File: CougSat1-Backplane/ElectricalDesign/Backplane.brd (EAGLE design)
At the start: 82.8 x 86 mm, 17 parts, among them J1 CougSat Socket, J10 CougSat Socket, J2 CougSat Socket, J3 CougSat Socket, J4 CougSat Socket, J5 Separation Switch, J6 Separation Switch, J7 CougSat Socket, J8 CougSat Socket, J9 CougSat Socket

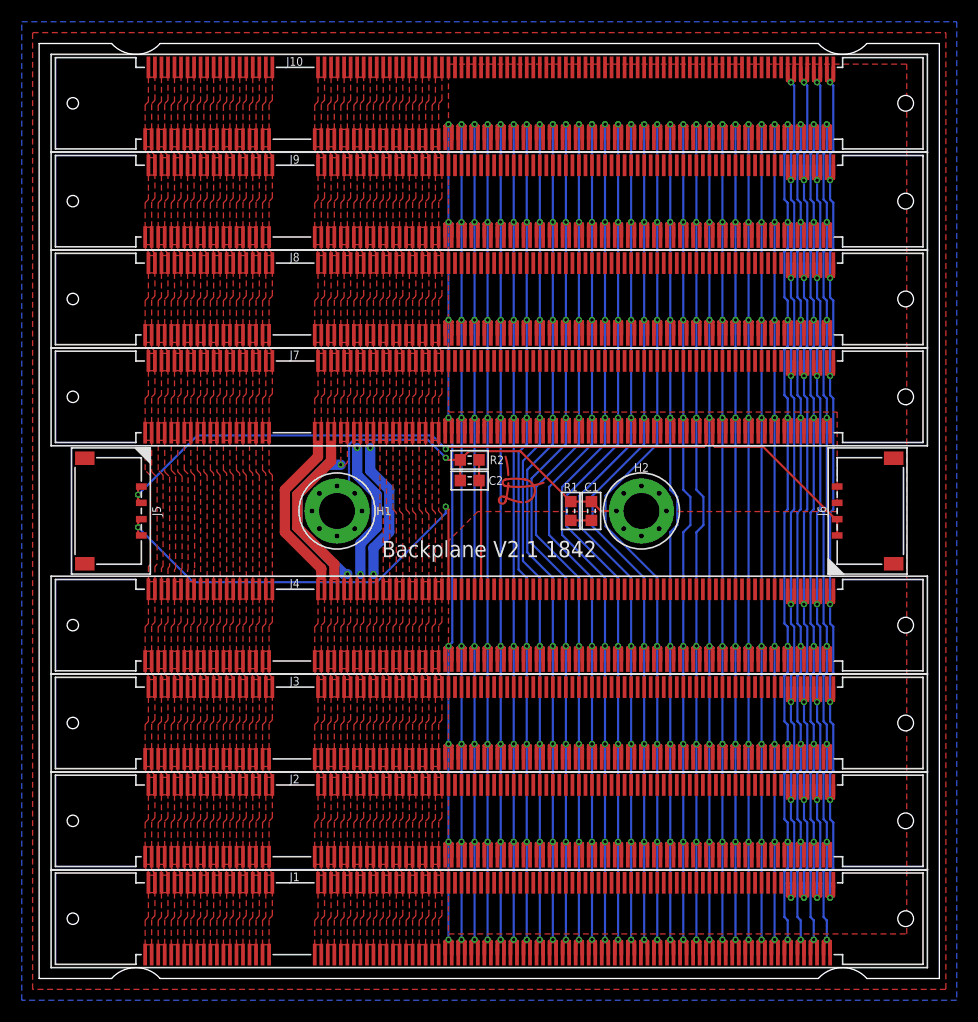
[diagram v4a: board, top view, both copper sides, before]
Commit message: Changed Cutout for Solar Panel Mount
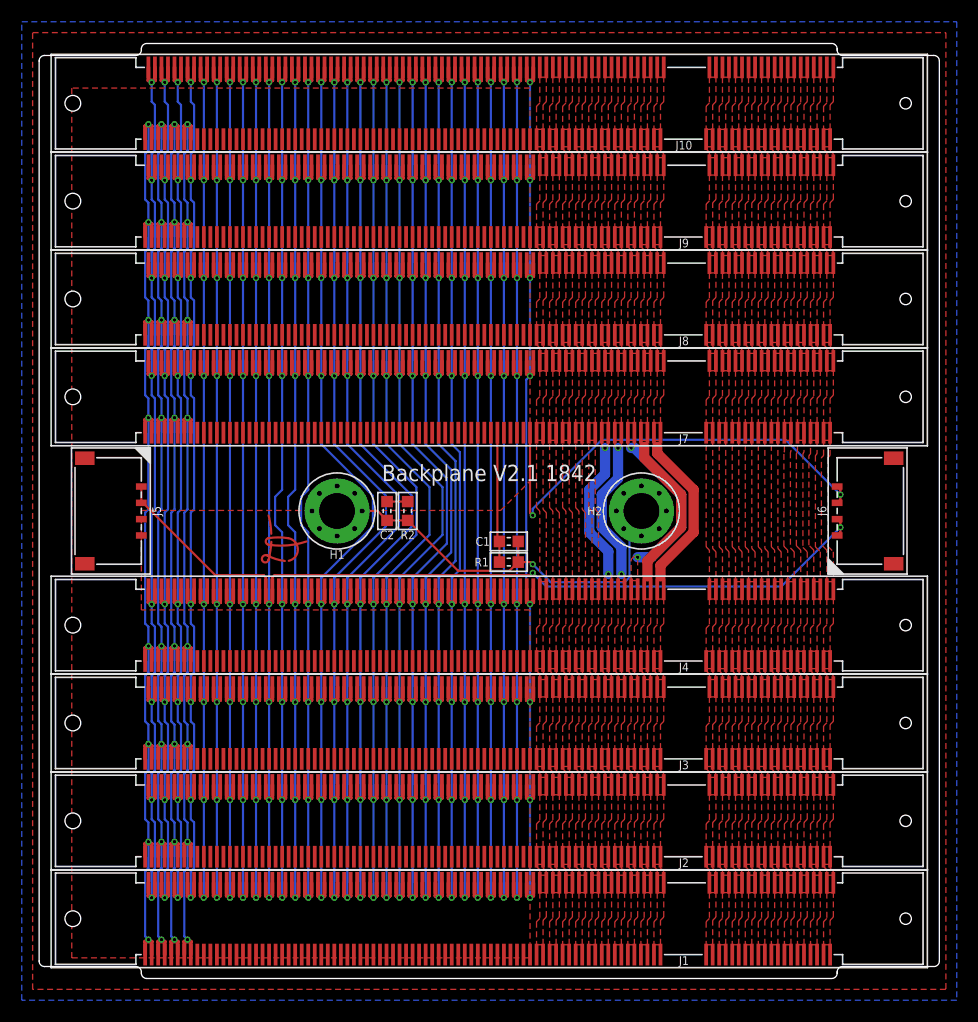
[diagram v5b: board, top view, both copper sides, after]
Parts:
- moved LOGO1 22.5 mm to (-18.8, -2.60)
- moved C1 8.10 mm to (1.80, -2.80), turned to 180 degrees
- moved C2 8.10 mm to (-9.40, 0.00), turned to 90 degrees
- moved R1 7.39 mm to (1.80, -4.70), turned to 0 degrees
- moved R2 7.39 mm to (-7.50, 0.00), turned to 270 degrees
- turned H1 to 180 degrees
- turned H2 to 180 degrees
- turned J1 to 180 degrees
- turned J10 to 180 degrees
- turned J2 to 180 degrees
- turned J3 to 180 degrees
- turned J4 to 180 degrees
- turned J7 to 180 degrees
- turned J8 to 180 degrees
- turned J9 to 180 degrees
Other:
- outline, holes or cut-outs redrawn

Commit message: Merge branch 'master' into panel+X
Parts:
- added LOGO100, LOGO3: Satellite 16mm, CougsInSpace-Aesthetics:CIS-SATELLITE-16
- added LOGO2: SIGNATUREHENDRIK, CougsInSpace-Aesthetics:SIGN-HENDRIK
- J1, J10, J2, J3, J4, J7, J8, J9: device CougsInSpace-Connectors:SODIMM-DDR1 -> CougsInSpace-Connectors:PCIE-8
- LOGO1: value SIGNATUREBRADLEY -> Text; device CougsInSpace-Aesthetics:SIGN-BRADLEY -> CougsInSpace-Aesthetics:CIS-TEXT
- moved J1 78.7 mm to (24.0, 37.5)
- moved J10 78.7 mm to (24.0, -37.5)
- moved J2 61.8 mm to (24.0, 28.5)
- moved J9 61.8 mm to (24.0, -28.5)
- moved J3 45.8 mm to (24.0, 19.5)
- moved J8 45.8 mm to (24.0, -19.5)
- moved J4 31.9 mm to (24.0, 10.5)
- moved J7 31.9 mm to (24.0, -10.5)
- moved C2 19.0 mm to (9.50, -1.80), turned to 270 degrees
- moved R2 17.1 mm to (9.50, 1.80)
- moved R1 13.0 mm to (-9.50, 1.80), turned to 270 degrees
- moved C1 11.3 mm to (-9.50, -1.80), turned to 270 degrees
- moved LOGO1 9.97 mm to (-28.4, 0.10), flipped to the bottom, turned to 90 degrees
- moved J5 3.00 mm to (-29.0, 0.00)
- moved J6 3.00 mm to (29.0, 0.00)
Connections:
- removed net CHASSIS: C1.1, C2.1, H1.1, H1.V1, H1.V2, H1.V3, H1.V4, H1.V5, H1.V6, H1.V7, H1.V8, H2.1, H2.V1, H2.V2, H2.V3, H2.V4, H2.V5, H2.V6, H2.V7, H2.V8, R1.2, R2.2
- removed net GPIO-6: J1.105, J1.107, J10.105, J10.107, J2.105, J2.107, J3.105, J3.107, J4.105, J4.107, J7.105, J7.107, J8.105, J8.107, J9.105, J9.107
- removed net GPIO-7: J1.109, J1.111, J10.109, J10.111, J2.109, J2.111, J3.109, J3.111, J4.109, J4.111, J7.109, J7.111, J8.109, J8.111, J9.109, J9.111
- removed net GPIO-8: J1.113, J1.115, J10.113, J10.115, J2.113, J2.115, J3.113, J3.115, J4.113, J4.115, J7.113, J7.115, J8.113, J8.115, J9.113, J9.115
- removed net GPIO-9: J1.117, J1.119, J10.117, J10.119, J2.117, J2.119, J3.117, J3.119, J4.117, J4.119, J7.117, J7.119, J8.117, J8.119, J9.117, J9.119
- new net CHASSIS1: C1.1, H1.1, H1.V1, H1.V2, H1.V3, H1.V4, H1.V5, H1.V6, H1.V7, H1.V8, R1.2
- new net CHASSIS2: C2.1, H2.1, H2.V1, H2.V2, H2.V3, H2.V4, H2.V5, H2.V6, H2.V7, H2.V8, R2.2
- net BUS_I2C0_IRQ: now also J1.A45, J1.B45, J10.A45, J10.B45, J2.A45, J2.B45, J3.A45, J3.B45, J4.A45, J4.B45, J7.A45, J7.B45, J8.A45, J8.B45, J9.A45, J9.B45; no longer J1.181, J1.183, J10.181, J10.183, J2.181, J2.183, J3.181, J3.183, J4.181, J4.183, J7.181, J7.183, J8.181, J8.183, J9.181, J9.183
- net BUS_I2C0_SCL: now also J1.A44, J1.B44, J10.A44, J10.B44, J2.A44, J2.B44, J3.A44, J3.B44, J4.A44, J4.B44, J7.A44, J7.B44, J8.A44, J8.B44, J9.A44, J9.B44; no longer J1.177, J1.179, J10.177, J10.179, J2.177, J2.179, J3.177, J3.179, J4.177, J4.179, J7.177, J7.179, J8.177, J8.179, J9.177, J9.179
- net BUS_I2C0_SDA: now also J1.A43, J1.B43, J10.A43, J10.B43, J2.A43, J2.B43, J3.A43, J3.B43, J4.A43, J4.B43, J7.A43, J7.B43, J8.A43, J8.B43, J9.A43, J9.B43; no longer J1.173, J1.175, J10.173, J10.175, J2.173, J2.175, J3.173, J3.175, J4.173, J4.175, J7.173, J7.175, J8.173, J8.175, J9.173, J9.175
- net BUS_I2C1_IRQ: now also J1.A32, J1.B32, J10.A32, J10.B32, J2.A32, J2.B32, J3.A32, J3.B32, J4.A32, J4.B32, J7.A32, J7.B32, J8.A32, J8.B32, J9.A32, J9.B32; no longer J1.129, J1.131, J10.129, J10.131, J2.129, J2.131, J3.129, J3.131, J4.129, J4.131, J7.129, J7.131, J8.129, J8.131, J9.129, J9.131
- net BUS_I2C1_SCL: now also J1.A31, J1.B31, J10.A31, J10.B31, J2.A31, J2.B31, J3.A31, J3.B31, J4.A31, J4.B31, J7.A31, J7.B31, J8.A31, J8.B31, J9.A31, J9.B31; no longer J1.125, J1.127, J10.125, J10.127, J2.125, J2.127, J3.125, J3.127, J4.125, J4.127, J7.125, J7.127, J8.125, J8.127, J9.125, J9.127
- net BUS_I2C1_SDA: now also J1.A30, J1.B30, J10.A30, J10.B30, J2.A30, J2.B30, J3.A30, J3.B30, J4.A30, J4.B30, J7.A30, J7.B30, J8.A30, J8.B30, J9.A30, J9.B30; no longer J1.121, J1.123, J10.121, J10.123, J2.121, J2.123, J3.121, J3.123, J4.121, J4.123, J7.121, J7.123, J8.121, J8.123, J9.121, J9.123
- net BUS_JTAG_EN-0: now also J1.B46, J10.B46, J2.B46, J3.B46, J4.B46, J7.B46, J8.B46, J9.B46; no longer J1.186, J1.188, J10.186, J10.188, J2.186, J2.188, J3.186, J3.188, J4.186, J4.188, J7.186, J7.188, J8.186, J8.188, J9.186, J9.188
- net BUS_JTAG_EN-1: now also J1.B47, J10.B47, J2.B47, J3.B47, J4.B47, J7.B47, J8.B47, J9.B47; no longer J1.190, J1.192, J10.190, J10.192, J2.190, J2.192, J3.190, J3.192, J4.190, J4.192, J7.190, J7.192, J8.190, J8.192, J9.190, J9.192
- net BUS_JTAG_EN-2: now also J1.B48, J10.B48, J2.B48, J3.B48, J4.B48, J7.B48, J8.B48, J9.B48; no longer J1.194, J1.196, J10.194, J10.196, J2.194, J2.196, J3.194, J3.196, J4.194, J4.196, J7.194, J7.196, J8.194, J8.196, J9.194, J9.196
- net BUS_JTAG_EN-3: now also J1.B49, J10.B49, J2.B49, J3.B49, J4.B49, J7.B49, J8.B49, J9.B49; no longer J1.198, J1.200, J10.198, J10.200, J2.198, J2.200, J3.198, J3.200, J4.198, J4.200, J7.198, J7.200, J8.198, J8.200, J9.198, J9.200
- net BUS_JTAG_TCK: now also J1.A46, J10.A46, J2.A46, J3.A46, J4.A46, J7.A46, J8.A46, J9.A46; no longer J1.185, J1.187, J10.185, J10.187, J2.185, J2.187, J3.185, J3.187, J4.185, J4.187, J7.185, J7.187, J8.185, J8.187, J9.185, J9.187
- net BUS_JTAG_TDI: now also J1.A47, J10.A47, J2.A47, J3.A47, J4.A47, J7.A47, J8.A47, J9.A47; no longer J1.189, J1.191, J10.189, J10.191, J2.189, J2.191, J3.189, J3.191, J4.189, J4.191, J7.189, J7.191, J8.189, J8.191, J9.189, J9.191
- net BUS_JTAG_TDO: now also J1.A48, J10.A48, J2.A48, J3.A48, J4.A48, J7.A48, J8.A48, J9.A48; no longer J1.193, J1.195, J10.193, J10.195, J2.193, J2.195, J3.193, J3.195, J4.193, J4.195, J7.193, J7.195, J8.193, J8.195, J9.193, J9.195
- net BUS_JTAG_TMS: now also J1.A49, J10.A49, J2.A49, J3.A49, J4.A49, J7.A49, J8.A49, J9.A49; no longer J1.197, J1.199, J10.197, J10.199, J2.197, J2.199, J3.197, J3.199, J4.197, J4.199, J7.197, J7.199, J8.197, J8.199, J9.197, J9.199
- net BUS_SPI_MISO: now also J1.A38, J1.B38, J10.A38, J10.B38, J2.A38, J2.B38, J3.A38, J3.B38, J4.A38, J4.B38, J7.A38, J7.B38, J8.A38, J8.B38, J9.A38, J9.B38; no longer J1.153, J1.155, J10.153, J10.155, J2.153, J2.155, J3.153, J3.155, J4.153, J4.155, J7.153, J7.155, J8.153, J8.155, J9.153, J9.155
- net BUS_SPI_MOSI: now also J1.A39, J1.B39, J10.A39, J10.B39, J2.A39, J2.B39, J3.A39, J3.B39, J4.A39, J4.B39, J7.A39, J7.B39, J8.A39, J8.B39, J9.A39, J9.B39; no longer J1.157, J1.159, J10.157, J10.159, J2.157, J2.159, J3.157, J3.159, J4.157, J4.159, J7.157, J7.159, J8.157, J8.159, J9.157, J9.159
- net BUS_SPI_SCK: now also J1.A37, J1.B37, J10.A37, J10.B37, J2.A37, J2.B37, J3.A37, J3.B37, J4.A37, J4.B37, J7.A37, J7.B37, J8.A37, J8.B37, J9.A37, J9.B37; no longer J1.149, J1.151, J10.149, J10.151, J2.149, J2.151, J3.149, J3.151, J4.149, J4.151, J7.149, J7.151, J8.149, J8.151, J9.149, J9.151
- net COM_SPI_CS: now also J1.A36, J1.B36, J10.A36, J10.B36, J2.A36, J2.B36, J3.A36, J3.B36, J4.A36, J4.B36, J7.A36, J7.B36, J8.A36, J8.B36, J9.A36, J9.B36; no longer J1.145, J1.147, J10.145, J10.147, J2.145, J2.147, J3.145, J3.147, J4.145, J4.147, J7.145, J7.147, J8.145, J8.147, J9.145, J9.147
- net COM_SPI_MISO: now also J1.A34, J1.B34, J10.A34, J10.B34, J2.A34, J2.B34, J3.A34, J3.B34, J4.A34, J4.B34, J7.A34, J7.B34, J8.A34, J8.B34, J9.A34, J9.B34; no longer J1.137, J1.139, J10.137, J10.139, J2.137, J2.139, J3.137, J3.139, J4.137, J4.139, J7.137, J7.139, J8.137, J8.139, J9.137, J9.139
- net COM_SPI_MOSI: now also J1.A35, J1.B35, J10.A35, J10.B35, J2.A35, J2.B35, J3.A35, J3.B35, J4.A35, J4.B35, J7.A35, J7.B35, J8.A35, J8.B35, J9.A35, J9.B35; no longer J1.141, J1.143, J10.141, J10.143, J2.141, J2.143, J3.141, J3.143, J4.141, J4.143, J7.141, J7.143, J8.141, J8.143, J9.141, J9.143
- net COM_SPI_SCK: now also J1.A33, J1.B33, J10.A33, J10.B33, J2.A33, J2.B33, J3.A33, J3.B33, J4.A33, J4.B33, J7.A33, J7.B33, J8.A33, J8.B33, J9.A33, J9.B33; no longer J1.133, J1.135, J10.133, J10.135, J2.133, J2.135, J3.133, J3.135, J4.133, J4.135, J7.133, J7.135, J8.133, J8.135, J9.133, J9.135
- net CTRL_!RESET: now also J1.A41, J1.B41, J10.A41, J10.B41, J2.A41, J2.B41, J3.A41, J3.B41, J4.A41, J4.B41, J7.A41, J7.B41, J8.A41, J8.B41, J9.A41, J9.B41; no longer J1.165, J1.167, J10.165, J10.167, J2.165, J2.167, J3.165, J3.167, J4.165, J4.167, J7.165, J7.167, J8.165, J8.167, J9.165, J9.167
- net CTRL_SYNC: now also J1.A42, J1.B42, J10.A42, J10.B42, J2.A42, J2.B42, J3.A42, J3.B42, J4.A42, J4.B42, J7.A42, J7.B42, J8.A42, J8.B42, J9.A42, J9.B42; no longer J1.169, J1.171, J10.169, J10.171, J2.169, J2.171, J3.169, J3.171, J4.169, J4.171, J7.169, J7.171, J8.169, J8.171, J9.169, J9.171
- net GPIO-0: now also J1.A24, J10.A24, J2.A24, J3.A24, J4.A24, J7.A24, J8.A24, J9.A24; no longer J1.81, J1.83, J10.81, J10.83, J2.81, J2.83, J3.81, J3.83, J4.81, J4.83, J7.81, J7.83, J8.81, J8.83, J9.81, J9.83
- net GPIO-1: now also J1.A25, J10.A25, J2.A25, J3.A25, J4.A25, J7.A25, J8.A25, J9.A25; no longer J1.85, J1.87, J10.85, J10.87, J2.85, J2.87, J3.85, J3.87, J4.85, J4.87, J7.85, J7.87, J8.85, J8.87, J9.85, J9.87
- net GPIO-2: now also J1.A26, J10.A26, J2.A26, J3.A26, J4.A26, J7.A26, J8.A26, J9.A26; no longer J1.89, J1.91, J10.89, J10.91, J2.89, J2.91, J3.89, J3.91, J4.89, J4.91, J7.89, J7.91, J8.89, J8.91, J9.89, J9.91
- net GPIO-3: now also J1.A27, J10.A27, J2.A27, J3.A27, J4.A27, J7.A27, J8.A27, J9.A27; no longer J1.93, J1.95, J10.93, J10.95, J2.93, J2.95, J3.93, J3.95, J4.93, J4.95, J7.93, J7.95, J8.93, J8.95, J9.93, J9.95
- net GPIO-4: now also J1.A28, J10.A28, J2.A28, J3.A28, J4.A28, J7.A28, J8.A28, J9.A28; no longer J1.97, J1.99, J10.97, J10.99, J2.97, J2.99, J3.97, J3.99, J4.97, J4.99, J7.97, J7.99, J8.97, J8.99, J9.97, J9.99
- net GPIO-5: now also J1.A29, J10.A29, J2.A29, J3.A29, J4.A29, J7.A29, J8.A29, J9.A29; no longer J1.101, J1.103, J10.101, J10.103, J2.101, J2.103, J3.101, J3.103, J4.101, J4.103, J7.101, J7.103, J8.101, J8.103, J9.101, J9.103
- net PGND: now also J1.A21, J1.A22, J1.A23, J1.B21, J1.B22, J1.B23, J1.B24, J1.B25, J1.B26, J1.B27, J1.B28, J1.B29, J10.A21, J10.A22, J10.A23, J10.B21, J10.B22, J10.B23, J10.B24, J10.B25, J10.B26, J10.B27, J10.B28, J10.B29, J2.A21, J2.A22, J2.A23, J2.B21, J2.B22, J2.B23, J2.B24, J2.B25, J2.B26, J2.B27, J2.B28, J2.B29, J3.A21, J3.A22, J3.A23, J3.B21, J3.B22, J3.B23, J3.B24, J3.B25, J3.B26, J3.B27, J3.B28, J3.B29, J4.A21, J4.A22, J4.A23, J4.B21, J4.B22, J4.B23, J4.B24, J4.B25, J4.B26, J4.B27, J4.B28, J4.B29, J7.A21, J7.A22, J7.A23, J7.B21, J7.B22, J7.B23, J7.B24, J7.B25, J7.B26, J7.B27, J7.B28, J7.B29, J8.A21, J8.A22, J8.A23, J8.B21, J8.B22, J8.B23, J8.B24, J8.B25, J8.B26, J8.B27, J8.B28, J8.B29, J9.A21, J9.A22, J9.A23, J9.B21, J9.B22, J9.B23, J9.B24, J9.B25, J9.B26, J9.B27, J9.B28, J9.B29; no longer J1.100, J1.102, J1.104, J1.106, J1.108, J1.110, J1.112, J1.114, J1.116, J1.118, J1.120, J1.122, J1.124, J1.126, J1.128, J1.130, J1.132, J1.134, J1.136, J1.138, J1.140, J1.142, J1.144, J1.146, J1.148, J1.150, J1.152, J1.154, J1.156, J1.158, J1.160, J1.162, J1.164, J1.166, J1.168, J1.170, J1.172, J1.174, J1.176, J1.178, J1.180, J1.182, J1.184, J1.82, J1.84, J1.86, J1.88, J1.90, J1.92, J1.94, J1.96, J1.98, J10.100, J10.102, J10.104, J10.106, J10.108, J10.110, J10.112, J10.114, J10.116, J10.118, J10.120, J10.122, J10.124, J10.126, J10.128, J10.130, J10.132, J10.134, J10.136, J10.138, J10.140, J10.142, J10.144, J10.146, J10.148, J10.150, J10.152, J10.154, J10.156, J10.158, J10.160, J10.162, J10.164, J10.166, J10.168, J10.170, J10.172, J10.174, J10.176, J10.178, J10.180, J10.182, J10.184, J10.82, J10.84, J10.86, J10.88, J10.90, J10.92, J10.94, J10.96, J10.98, J2.100, J2.102, J2.104, J2.106, J2.108, J2.110, J2.112, J2.114, J2.116, J2.118, J2.120, J2.122, J2.124, J2.126, J2.128, J2.130, J2.132, J2.134, J2.136, J2.138, J2.140, J2.142, J2.144, J2.146, J2.148, J2.150, J2.152, J2.154, J2.156, J2.158, J2.160, J2.162, J2.164, J2.166, J2.168, J2.170, J2.172, J2.174, J2.176, J2.178, J2.180, J2.182, J2.184, J2.82, J2.84, J2.86, J2.88, J2.90, J2.92, J2.94, J2.96, J2.98, J3.100, J3.102, J3.104, J3.106, J3.108, J3.110, J3.112, J3.114, J3.116, J3.118, J3.120, J3.122, J3.124, J3.126, J3.128, J3.130, J3.132, J3.134, J3.136, J3.138, J3.140, J3.142, J3.144, J3.146, J3.148, J3.150, J3.152, J3.154, J3.156, J3.158, J3.160, J3.162, J3.164, J3.166, J3.168, J3.170, J3.172, J3.174, J3.176, J3.178, J3.180, J3.182, J3.184, J3.82, J3.84, J3.86, J3.88, J3.90, J3.92, J3.94, J3.96, J3.98, J4.100, J4.102, J4.104, J4.106, J4.108, J4.110, J4.112, J4.114, J4.116, J4.118, J4.120, J4.122, J4.124, J4.126, J4.128, J4.130, J4.132, J4.134, J4.136, J4.138, J4.140, J4.142, J4.144, J4.146, J4.148, J4.150, J4.152, J4.154, J4.156, J4.158, J4.160, J4.162, J4.164, J4.166, J4.168, J4.170, J4.172, J4.174, J4.176, J4.178, J4.180, J4.182, J4.184, J4.82, J4.84, J4.86, J4.88, J4.90, J4.92, J4.94, J4.96, J4.98, J7.100, J7.102, J7.104, J7.106, J7.108, J7.110, J7.112, J7.114, J7.116, J7.118, J7.120, J7.122, J7.124, J7.126, J7.128, J7.130, J7.132, J7.134, J7.136, J7.138, J7.140, J7.142, J7.144, J7.146, J7.148, J7.150, J7.152, J7.154, J7.156, J7.158, J7.160, J7.162, J7.164, J7.166, J7.168, J7.170, J7.172, J7.174, J7.176, J7.178, J7.180, J7.182, J7.184, J7.82, J7.84, J7.86, J7.88, J7.90, J7.92, J7.94, J7.96, J7.98, J8.100, J8.102, J8.104, J8.106, J8.108, J8.110, J8.112, J8.114, J8.116, J8.118, J8.120, J8.122, J8.124, J8.126, J8.128, J8.130, J8.132, J8.134, J8.136, J8.138, J8.140, J8.142, J8.144, J8.146, J8.148, J8.150, J8.152, J8.154, J8.156, J8.158, J8.160, J8.162, J8.164, J8.166, J8.168, J8.170, J8.172, J8.174, J8.176, J8.178, J8.180, J8.182, J8.184, J8.82, J8.84, J8.86, J8.88, J8.90, J8.92, J8.94, J8.96, J8.98, J9.100, J9.102, J9.104, J9.106, J9.108, J9.110, J9.112, J9.114, J9.116, J9.118, J9.120, J9.122, J9.124, J9.126, J9.128, J9.130, J9.132, J9.134, J9.136, J9.138, J9.140, J9.142, J9.144, J9.146, J9.148, J9.150, J9.152, J9.154, J9.156, J9.158, J9.160, J9.162, J9.164, J9.166, J9.168, J9.170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
- net PR_3.3V-0: now also J1.A1, J1.B1, J10.A1, J10.B1, J2.A1, J2.B1, J3.A1, J3.B1, J4.A1, J4.B1, J7.A1, J7.B1, J8.A1, J8.B1, J9.A1, J9.B1; no longer J1.1, J1.2, J1.3, J1.4, J10.1, J10.2, J10.3, J10.4, J2.1, J2.2, J2.3, J2.4, J3.1, J3.2, J3.3, J3.4, J4.1, J4.2, J4.3, J4.4, J7.1, J7.2, J7.3, J7.4, J8.1, J8.2, J8.3, J8.4, J9.1, J9.2, J9.3, J9.4
- net PR_3.3V-1: now also J1.A2, J1.B2, J10.A2, J10.B2, J2.A2, J2.B2, J3.A2, J3.B2, J4.A2, J4.B2, J7.A2, J7.B2, J8.A2, J8.B2, J9.A2, J9.B2; no longer J1.5, J1.6, J1.7, J1.8, J10.5, J10.6, J10.7, J10.8, J2.5, J2.6, J2.7, J2.8, J3.5, J3.6, J3.7, J3.8, J4.5, J4.6, J4.7, J4.8, J7.5, J7.6, J7.7, J7.8, J8.5, J8.6, J8.7, J8.8, J9.5, J9.6, J9.7, J9.8
- net PR_3.3V-10: now also J1.A11, J1.B11, J10.A11, J10.B11, J2.A11, J2.B11, J3.A11, J3.B11, J4.A11, J4.B11, J7.A11, J7.B11, J8.A11, J8.B11, J9.A11, J9.B11; no longer J1.41, J1.42, J1.43, J1.44, J10.41, J10.42, J10.43, J10.44, J2.41, J2.42, J2.43, J2.44, J3.41, J3.42, J3.43, J3.44, J4.41, J4.42, J4.43, J4.44, J7.41, J7.42, J7.43, J7.44, J8.41, J8.42, J8.43, J8.44, J9.41, J9.42, J9.43, J9.44
- net PR_3.3V-11: now also J1.A12, J1.B12, J10.A12, J10.B12, J2.A12, J2.B12, J3.A12, J3.B12, J4.A12, J4.B12, J7.A12, J7.B12, J8.A12, J8.B12, J9.A12, J9.B12; no longer J1.45, J1.46, J1.47, J1.48, J10.45, J10.46, J10.47, J10.48, J2.45, J2.46, J2.47, J2.48, J3.45, J3.46, J3.47, J3.48, J4.45, J4.46, J4.47, J4.48, J7.45, J7.46, J7.47, J7.48, J8.45, J8.46, J8.47, J8.48, J9.45, J9.46, J9.47, J9.48
- net PR_3.3V-12: now also J1.A13, J1.B13, J10.A13, J10.B13, J2.A13, J2.B13, J3.A13, J3.B13, J4.A13, J4.B13, J7.A13, J7.B13, J8.A13, J8.B13, J9.A13, J9.B13; no longer J1.49, J1.50, J1.51, J1.52, J10.49, J10.50, J10.51, J10.52, J2.49, J2.50, J2.51, J2.52, J3.49, J3.50, J3.51, J3.52, J4.49, J4.50, J4.51, J4.52, J7.49, J7.50, J7.51, J7.52, J8.49, J8.50, J8.51, J8.52, J9.49, J9.50, J9.51, J9.52
- net PR_3.3V-2: now also J1.A3, J1.B3, J10.A3, J10.B3, J2.A3, J2.B3, J3.A3, J3.B3, J4.A3, J4.B3, J7.A3, J7.B3, J8.A3, J8.B3, J9.A3, J9.B3; no longer J1.10, J1.11, J1.12, J1.9, J10.10, J10.11, J10.12, J10.9, J2.10, J2.11, J2.12, J2.9, J3.10, J3.11, J3.12, J3.9, J4.10, J4.11, J4.12, J4.9, J7.10, J7.11, J7.12, J7.9, J8.10, J8.11, J8.12, J8.9, J9.10, J9.11, J9.12, J9.9
- net PR_3.3V-3: now also J1.A4, J1.B4, J10.A4, J10.B4, J2.A4, J2.B4, J3.A4, J3.B4, J4.A4, J4.B4, J7.A4, J7.B4, J8.A4, J8.B4, J9.A4, J9.B4; no longer J1.13, J1.14, J1.15, J1.16, J10.13, J10.14, J10.15, J10.16, J2.13, J2.14, J2.15, J2.16, J3.13, J3.14, J3.15, J3.16, J4.13, J4.14, J4.15, J4.16, J7.13, J7.14, J7.15, J7.16, J8.13, J8.14, J8.15, J8.16, J9.13, J9.14, J9.15, J9.16
- net PR_3.3V-4: now also J1.A5, J1.B5, J10.A5, J10.B5, J2.A5, J2.B5, J3.A5, J3.B5, J4.A5, J4.B5, J7.A5, J7.B5, J8.A5, J8.B5, J9.A5, J9.B5; no longer J1.17, J1.18, J1.19, J1.20, J10.17, J10.18, J10.19, J10.20, J2.17, J2.18, J2.19, J2.20, J3.17, J3.18, J3.19, J3.20, J4.17, J4.18, J4.19, J4.20, J7.17, J7.18, J7.19, J7.20, J8.17, J8.18, J8.19, J8.20, J9.17, J9.18, J9.19, J9.20
- net PR_3.3V-5: now also J1.A6, J1.B6, J10.A6, J10.B6, J2.A6, J2.B6, J3.A6, J3.B6, J4.A6, J4.B6, J7.A6, J7.B6, J8.A6, J8.B6, J9.A6, J9.B6; no longer J1.21, J1.22, J1.23, J1.24, J10.21, J10.22, J10.23, J10.24, J2.21, J2.22, J2.23, J2.24, J3.21, J3.22, J3.23, J3.24, J4.21, J4.22, J4.23, J4.24, J7.21, J7.22, J7.23, J7.24, J8.21, J8.22, J8.23, J8.24, J9.21, J9.22, J9.23, J9.24
- net PR_3.3V-6: now also J1.A7, J1.B7, J10.A7, J10.B7, J2.A7, J2.B7, J3.A7, J3.B7, J4.A7, J4.B7, J7.A7, J7.B7, J8.A7, J8.B7, J9.A7, J9.B7; no longer J1.25, J1.26, J1.27, J1.28, J10.25, J10.26, J10.27, J10.28, J2.25, J2.26, J2.27, J2.28, J3.25, J3.26, J3.27, J3.28, J4.25, J4.26, J4.27, J4.28, J7.25, J7.26, J7.27, J7.28, J8.25, J8.26, J8.27, J8.28, J9.25, J9.26, J9.27, J9.28
- net PR_3.3V-7: now also J1.A8, J1.B8, J10.A8, J10.B8, J2.A8, J2.B8, J3.A8, J3.B8, J4.A8, J4.B8, J7.A8, J7.B8, J8.A8, J8.B8, J9.A8, J9.B8; no longer J1.29, J1.30, J1.31, J1.32, J10.29, J10.30, J10.31, J10.32, J2.29, J2.30, J2.31, J2.32, J3.29, J3.30, J3.31, J3.32, J4.29, J4.30, J4.31, J4.32, J7.29, J7.30, J7.31, J7.32, J8.29, J8.30, J8.31, J8.32, J9.29, J9.30, J9.31, J9.32
- net PR_3.3V-8: now also J1.A9, J1.B9, J10.A9, J10.B9, J2.A9, J2.B9, J3.A9, J3.B9, J4.A9, J4.B9, J7.A9, J7.B9, J8.A9, J8.B9, J9.A9, J9.B9; no longer J1.33, J1.34, J1.35, J1.36, J10.33, J10.34, J10.35, J10.36, J2.33, J2.34, J2.35, J2.36, J3.33, J3.34, J3.35, J3.36, J4.33, J4.34, J4.35, J4.36, J7.33, J7.34, J7.35, J7.36, J8.33, J8.34, J8.35, J8.36, J9.33, J9.34, J9.35, J9.36
- net PR_3.3V-9: now also J1.A10, J1.B10, J10.A10, J10.B10, J2.A10, J2.B10, J3.A10, J3.B10, J4.A10, J4.B10, J7.A10, J7.B10, J8.A10, J8.B10, J9.A10, J9.B10; no longer J1.37, J1.38, J1.39, J1.40, J10.37, J10.38, J10.39, J10.40, J2.37, J2.38, J2.39, J2.40, J3.37, J3.38, J3.39, J3.40, J4.37, J4.38, J4.39, J4.40, J7.37, J7.38, J7.39, J7.40, J8.37, J8.38, J8.39, J8.40, J9.37, J9.38, J9.39, J9.40
- net PR_BATT-0: now also J1.A14, J1.B14, J10.A14, J10.B14, J2.A14, J2.B14, J3.A14, J3.B14, J4.A14, J4.B14, J7.A14, J7.B14, J8.A14, J8.B14, J9.A14, J9.B14; no longer J1.53, J1.54, J1.55, J1.56, J10.53, J10.54, J10.55, J10.56, J2.53, J2.54, J2.55, J2.56, J3.53, J3.54, J3.55, J3.56, J4.53, J4.54, J4.55, J4.56, J7.53, J7.54, J7.55, J7.56, J8.53, J8.54, J8.55, J8.56, J9.53, J9.54, J9.55, J9.56
- net PR_BATT-1: now also J1.A15, J1.B15, J10.A15, J10.B15, J2.A15, J2.B15, J3.A15, J3.B15, J4.A15, J4.B15, J7.A15, J7.B15, J8.A15, J8.B15, J9.A15, J9.B15; no longer J1.57, J1.58, J1.59, J1.60, J10.57, J10.58, J10.59, J10.60, J2.57, J2.58, J2.59, J2.60, J3.57, J3.58, J3.59, J3.60, J4.57, J4.58, J4.59, J4.60, J7.57, J7.58, J7.59, J7.60, J8.57, J8.58, J8.59, J8.60, J9.57, J9.58, J9.59, J9.60
- net PR_BATT-2: now also J1.A16, J1.B16, J10.A16, J10.B16, J2.A16, J2.B16, J3.A16, J3.B16, J4.A16, J4.B16, J7.A16, J7.B16, J8.A16, J8.B16, J9.A16, J9.B16; no longer J1.61, J1.62, J1.63, J1.64, J10.61, J10.62, J10.63, J10.64, J2.61, J2.62, J2.63, J2.64, J3.61, J3.62, J3.63, J3.64, J4.61, J4.62, J4.63, J4.64, J7.61, J7.62, J7.63, J7.64, J8.61, J8.62, J8.63, J8.64, J9.61, J9.62, J9.63, J9.64
- net PR_BATT-3: now also J1.A17, J1.B17, J10.A17, J10.B17, J2.A17, J2.B17, J3.A17, J3.B17, J4.A17, J4.B17, J7.A17, J7.B17, J8.A17, J8.B17, J9.A17, J9.B17; no longer J1.65, J1.66, J1.67, J1.68, J10.65, J10.66, J10.67, J10.68, J2.65, J2.66, J2.67, J2.68, J3.65, J3.66, J3.67, J3.68, J4.65, J4.66, J4.67, J4.68, J7.65, J7.66, J7.67, J7.68, J8.65, J8.66, J8.67, J8.68, J9.65, J9.66, J9.67, J9.68
- net PR_BATT-4: now also J1.A18, J1.B18, J10.A18, J10.B18, J2.A18, J2.B18, J3.A18, J3.B18, J4.A18, J4.B18, J7.A18, J7.B18, J8.A18, J8.B18, J9.A18, J9.B18; no longer J1.69, J1.70, J1.71, J1.72, J10.69, J10.70, J10.71, J10.72, J2.69, J2.70, J2.71, J2.72, J3.69, J3.70, J3.71, J3.72, J4.69, J4.70, J4.71, J4.72, J7.69, J7.70, J7.71, J7.72, J8.69, J8.70, J8.71, J8.72, J9.69, J9.70, J9.71, J9.72
- net PR_BATT-5: now also J1.A19, J1.B19, J10.A19, J10.B19, J2.A19, J2.B19, J3.A19, J3.B19, J4.A19, J4.B19, J7.A19, J7.B19, J8.A19, J8.B19, J9.A19, J9.B19; no longer J1.73, J1.74, J1.75, J1.76, J10.73, J10.74, J10.75, J10.76, J2.73, J2.74, J2.75, J2.76, J3.73, J3.74, J3.75, J3.76, J4.73, J4.74, J4.75, J4.76, J7.73, J7.74, J7.75, J7.76, J8.73, J8.74, J8.75, J8.76, J9.73, J9.74, J9.75, J9.76
- net PR_BATT-6: now also J1.A20, J1.B20, J10.A20, J10.B20, J2.A20, J2.B20, J3.A20, J3.B20, J4.A20, J4.B20, J7.A20, J7.B20, J8.A20, J8.B20, J9.A20, J9.B20; no longer J1.77, J1.78, J1.79, J1.80, J10.77, J10.78, J10.79, J10.80, J2.77, J2.78, J2.79, J2.80, J3.77, J3.78, J3.79, J3.80, J4.77, J4.78, J4.79, J4.80, J7.77, J7.78, J7.79, J7.80, J8.77, J8.78, J8.79, J8.80, J9.77, J9.78, J9.79, J9.80
- net PWR_CTRL_SW: now also J1.A40, J1.B40, J10.A40, J10.B40, J2.A40, J2.B40, J3.A40, J3.B40, J4.A40, J4.B40, J7.A40, J7.B40, J8.A40, J8.B40, J9.A40, J9.B40; no longer J1.161, J1.163, J10.161, J10.163, J2.161, J2.163, J3.161, J3.163, J4.161, J4.163, J7.161, J7.163, J8.161, J8.163, J9.161, J9.163
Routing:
- net PGND: track 57.0 -> 382.0 mm, vias 2 -> 1
- net PR_BATT-2: track 0.00 -> 148.5 mm
- net PR_3.3V-9: track 0.00 -> 148.5 mm
- net PR_3.3V-7: track 0.00 -> 148.5 mm
- net PR_3.3V-5: track 0.00 -> 148.5 mm
- net PR_3.3V-3: track 0.00 -> 148.5 mm
- net PR_3.3V-1: track 0.00 -> 148.5 mm
- net PR_BATT-6: track 0.00 -> 144.4 mm
- net PR_BATT-4: track 0.00 -> 144.1 mm
- net PR_BATT-3: track 0.00 -> 136.5 mm
- net PR_3.3V-8: track 0.00 -> 136.5 mm
- net PR_3.3V-6: track 0.00 -> 136.5 mm
- net PR_3.3V-4: track 0.00 -> 136.5 mm
- net PR_3.3V-2: track 0.00 -> 136.5 mm
- net PR_3.3V-0: track 0.00 -> 136.5 mm
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- added copper zone on layer 16, net BALANCING-TOP
- added copper zone on layer 16, net PGND
- removed copper zone on layer 16, net BALANCING-BOTTOM
- removed copper zone on layer 1, net BUS_I2C0_IRQ
- removed copper zone on layer 1, net BUS_I2C0_SCL
- removed copper zone on layer 1, net BUS_I2C0_SDA
- removed copper zone on layer 1, net BUS_I2C1_IRQ
- removed copper zone on layer 1, net BUS_I2C1_SCL
- removed copper zone on layer 1, net BUS_I2C1_SDA
- removed copper zone on layer 1, net BUS_JTAG_EN-0
- removed copper zone on layer 1, net BUS_JTAG_EN-1
- removed copper zone on layer 1, net BUS_JTAG_EN-2
- removed copper zone on layer 1, net BUS_JTAG_EN-3
- removed copper zone on layer 1, net BUS_JTAG_TCK
- removed copper zone on layer 1, net BUS_JTAG_TDI
- removed copper zone on layer 1, net BUS_JTAG_TDO
- removed copper zone on layer 1, net BUS_JTAG_TMS
- removed copper zone on layer 1, net BUS_SPI_MISO
- removed copper zone on layer 1, net BUS_SPI_MOSI
- removed copper zone on layer 1, net BUS_SPI_SCK
- removed copper zone on layer 1, net COM_SPI_CS
- removed copper zone on layer 1, net COM_SPI_MISO
- removed copper zone on layer 1, net COM_SPI_MOSI
- removed copper zone on layer 1, net COM_SPI_SCK
- removed copper zone on layer 1, net CTRL_!RESET
- removed copper zone on layer 1, net CTRL_SYNC
- removed copper zone on layer 1, net GPIO-0
- removed copper zone on layer 1, net GPIO-1
- removed copper zone on layer 1, net GPIO-2
- removed copper zone on layer 1, net GPIO-3
- removed copper zone on layer 1, net GPIO-4
- removed copper zone on layer 1, net GPIO-5
- removed copper zone on layer 1, net GPIO-6
- removed copper zone on layer 1, net GPIO-7
- removed copper zone on layer 1, net GPIO-8
- removed copper zone on layer 1, net GPIO-9
- removed copper zone on layer 1, net PR_3.3V-0
- removed copper zone on layer 1, net PR_3.3V-1
- removed copper zone on layer 1, net PR_3.3V-10
- removed copper zone on layer 1, net PR_3.3V-11
- removed copper zone on layer 1, net PR_3.3V-12
- removed copper zone on layer 1, net PR_3.3V-2
- removed copper zone on layer 1, net PR_3.3V-3
- removed copper zone on layer 1, net PR_3.3V-4
- removed copper zone on layer 1, net PR_3.3V-5
- removed copper zone on layer 1, net PR_3.3V-6
- removed copper zone on layer 1, net PR_3.3V-7
- removed copper zone on layer 1, net PR_3.3V-8
- removed copper zone on layer 1, net PR_3.3V-9
- removed copper zone on layer 1, net PR_BATT-0
- removed copper zone on layer 1, net PR_BATT-1
- removed copper zone on layer 1, net PR_BATT-2
- removed copper zone on layer 1, net PR_BATT-3
- removed copper zone on layer 1, net PR_BATT-4
- removed copper zone on layer 1, net PR_BATT-5
- removed copper zone on layer 1, net PR_BATT-6
- removed copper zone on layer 1, net PWR_CTRL_SW
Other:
- outline, holes or cut-outs redrawn
- board text added: "Backplane V3.0"
- board text added: "Slot 0"
- board text added: "Slot 1"
- board text added: "Slot 2"
- board text added: "Slot 3"
- board text added: "Slot 4"
- board text added: "Slot 5"
- board text added: "Slot 6"
- board text added: "Slot 7"
- board text removed: "Backplane V2.1 1842"
